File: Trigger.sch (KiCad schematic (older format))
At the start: 2 parts

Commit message: more
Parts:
- added C1, C2: C_Small, symbol Device:C_Small
- added J2: ARM_SWD, symbol MyComponents:ARM_SWD
- added U1: MCP6002, symbol MyComponents:MCP6002
- J1: renamed from J?; symbol dk_USB-DVI-HDMI-Connectors:UE27AC54100 -> Trigger-rescue:UE27AC54100-dk_USB-DVI-HDMI-Connectors
- U2: renamed from U?; symbol MyComponents:SAMD21E -> Trigger-rescue:SAMD21E-MyComponents
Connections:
- net labels added: 3V3, 5V, GND-power
- wire segments 2 -> 19
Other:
- note added: "Close to IC"
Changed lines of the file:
@@
 EESchema Schematic File Version 4
+LIBS:Trigger-cache
 EELAYER 26 0
 EELAYER END
@@
 $EndDescr
 $Comp
-L MyComponents:SAMD21E U?
+L Trigger-rescue:SAMD21E-MyComponents U2
 U 1 1 5C325D69
 P 4650 3400
-F 0 "U?" H 4650 2014 50  0000 C CNN
+F 0 "U2" H 4650 2014 50  0000 C CNN
 F 1 "SAMD21E" H 4650 1923 50  0000 C CNN
 F 2 "" H 4500 4400 50  0001 C CNN
@@
 $EndComp
 $Comp
-L dk_USB-DVI-HDMI-Connectors:UE27AC54100 J?
+L Trigger-rescue:UE27AC54100-dk_USB-DVI-HDMI-Connectors J1
 U 1 1 5C3264C2
 P 950 3600
-F 0 "J?" H 1069 4112 60  0000 C CNN
+F 0 "J1" H 1069 4112 60  0000 C CNN
 F 1 "UE27AC54100" H 1069 4006 60  0000 C CNN
 F 2 "digikey-footprints:USB_A_Female_UE27AC54100" H 1150 3800 60  0001 L CNN
@@
 DP
 $Comp
-L power:GND #PWR?
+L Trigger-rescue:GND-power #PWR01
 U 1 1 5C326690
 P 1250 4750
-F 0 "#PWR?" H 1250 4500 50  0001 C CNN
+F 0 "#PWR01" H 1250 4500 50  0001 C CNN
 F 1 "GND" H 1255 4577 50  0000 C CNN
 F 2 "" H 1250 4750 50  0001 C CNN
@@
 Text Label 1250 4750 0    50   ~ 0
 GND
-Wire Wire Line
-	4400 4700 4300 4700
-Wire Wire Line
-	4300 4700 4300 4950
-Connection ~ 4300 4700
-Text Label 4300 4950 0    50   ~ 0
-GND
 Text Label 4200 2350 0    50   ~ 0
 GND
+$Comp
+L MyComponents:MCP6002 U1
+U 1 1 5C37B7AA
+P 2500 6200
+F 0 "U1" H 3041 6253 60  0000 L CNN
+F 1 "MCP6002" H 3041 6147 60  0000 L CNN
+F 2 "" H 2500 6200 60  0000 C CNN
+F 3 "" H 2500 6200 60  0000 C CNN
+	1    2500 6200
+	1    0    0    -1
+$EndComp
+$Comp
+L MyComponents:MCP6002 U1
+U 2 1 5C37B8E3
+P 4400 6200
+F 0 "U1" H 4941 6253 60  0000 L CNN
+F 1 "MCP6002" H 4941 6147 60  0000 L CNN
+F 2 "" H 4400 6200 60  0000 C CNN
+F 3 "" H 4400 6200 60  0000 C CNN
+	2    4400 6200
+	1    0    0    -1
+$EndComp
+$Comp
+L Trigger-rescue:GND-power #PWR02
+U 1 1 5C37B973
+P 3500 6800
+F 0 "#PWR02" H 3500 6550 50  0001 C CNN
+F 1 "GND-power" H 3505 6627 50  0000 C CNN
+F 2 "" H 3500 6800 50  0001 C CNN
+F 3 "" H 3500 6800 50  0001 C CNN
+	1    3500 6800
+	1    0    0    -1
+$EndComp
+Wire Wire Line
+	2400 6600 3500 6600
+Wire Wire Line
+	3500 6600 3500 6800
+Wire Wire Line
+	3500 6600 4300 6600
+Connection ~ 3500 6600
+Text Label 4300 6600 0    50   ~ 0
+GND
+$Comp
+L MyComponents:ARM_SWD J2
+U 1 1 5C37BEB5
+P 1100 1750
+F 0 "J2" H 956 2358 60  0000 C CNN
+F 1 "ARM_SWD" H 956 2252 60  0000 C CNN
+F 2 "" H 1100 1750 60  0000 C CNN
+F 3 "" H 1100 1750 60  0000 C CNN
+	1    1100 1750
+	1    0    0    -1
+$EndComp
+Wire Wire Line
+	1300 1400 1400 1400
+Wire Wire Line
+	1500 1600 1500 1800
+Wire Wire Line
+	1300 1800 1500 1800
+Wire Wire Line
+	1300 1600 1500 1600
+Wire Wire Line
+	1500 1800 1500 2000
+Wire Wire Line
+	1300 2000 1500 2000
+Connection ~ 1500 1800
+Text Label 1500 1800 0    50   ~ 0
+GND
+Text Label 1400 1400 0    50   ~ 0
+3V3
+Wire Wire Line
+	4100 2350 4000 2350
+Wire Wire Line
+	4000 2200 4000 2350
+Connection ~ 4000 2350
+Text Label 4000 2200 0    50   ~ 0
+3V3
+Wire Wire Line
+	4400 4700 4400 4750
+Text Label 4400 4750 0    50   ~ 0
+GND
+Wire Wire Line
+	4300 4700 4300 4750
+Text Label 4300 4750 2    50   ~ 0
+3V3
+$Comp
+L Device:C_Small C1
+U 1 1 5C37CBD9
+P 1200 4500
+F 0 "C1" H 1292 4546 50  0000 L CNN
+F 1 "C_Small" H 1292 4455 50  0000 L CNN
+F 2 "" H 1200 4500 50  0001 C CNN
+F 3 "~" H 1200 4500 50  0001 C CNN
+	1    1200 4500
+	1    0    0    -1
+$EndComp
+$Comp
+L Device:C_Small C2
+U 1 1 5C37CC39
+P 1600 4500
+F 0 "C2" H 1692 4546 50  0000 L CNN
+F 1 "C_Small" H 1692 4455 50  0000 L CNN
+F 2 "" H 1600 4500 50  0001 C CNN
+F 3 "~" H 1600 4500 50  0001 C CNN
+	1    1600 4500
+	1    0    0    -1
+$EndComp
+Wire Wire Line
+	1250 4750 1250 4600
+Wire Wire Line
+	1250 4600 1200 4600
+Wire Wire Line
+	1250 4600 1600 4600
+Connection ~ 1250 4600
+Wire Wire Line
+	1200 4400 1200 4350
+Wire Wire Line
+	1200 4350 1600 4350
+Wire Wire Line
+	1600 4350 1600 4400
+Text Label 1200 4350 2    50   ~ 0
+3V3
+Text Notes 1800 4300 2    59   ~ 0
+Close to IC
+Text Label 4300 5800 0    59   ~ 0
+5V
+Text Label 2400 5800 0    59   ~ 0
+5V
 $EndSCHEMATC

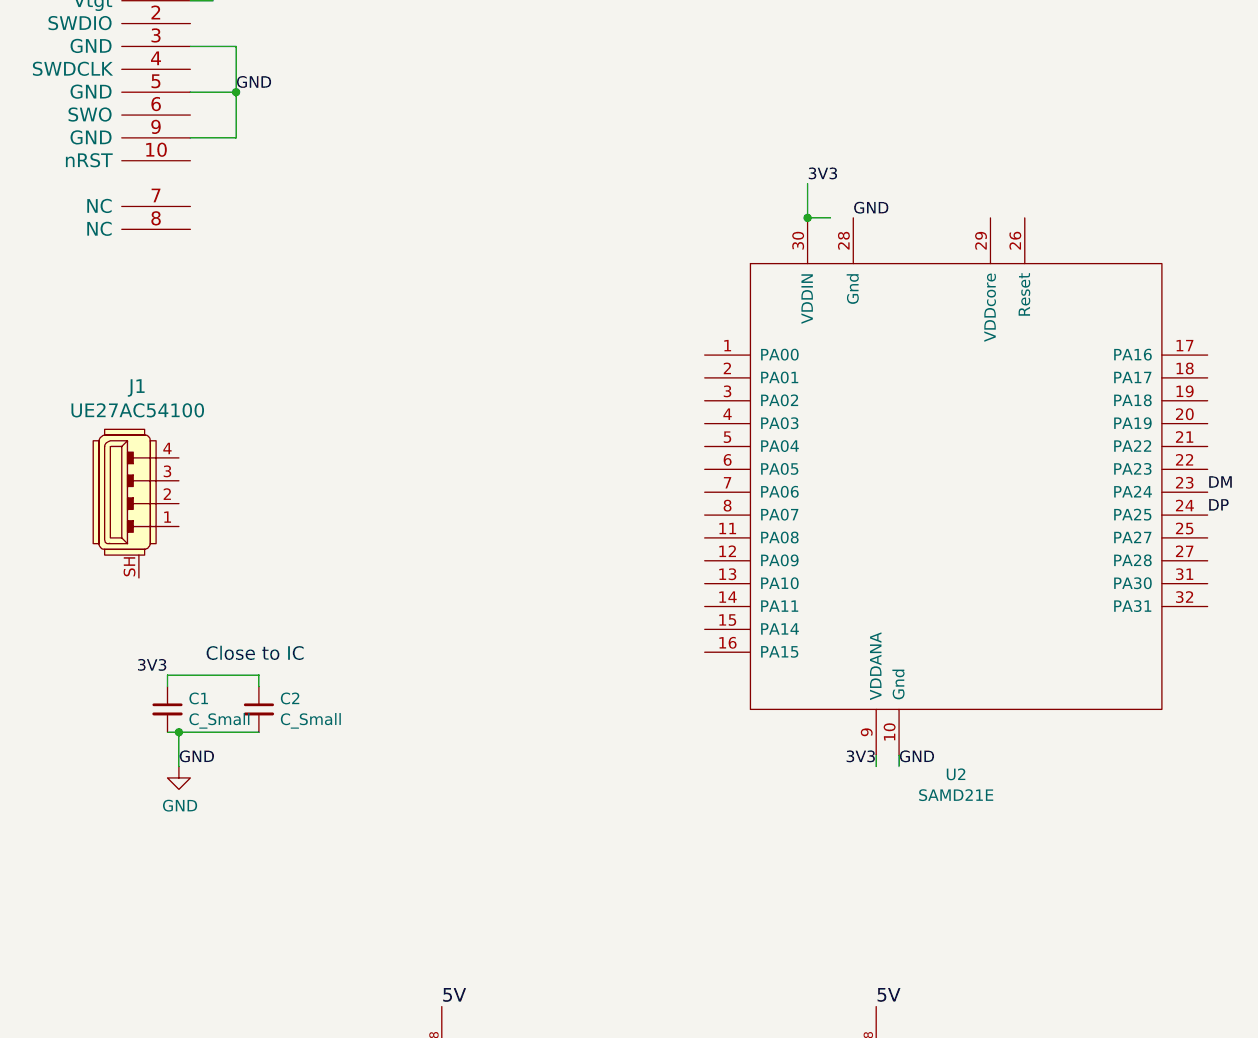
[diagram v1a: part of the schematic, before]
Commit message: corrected symbol samd and more connections
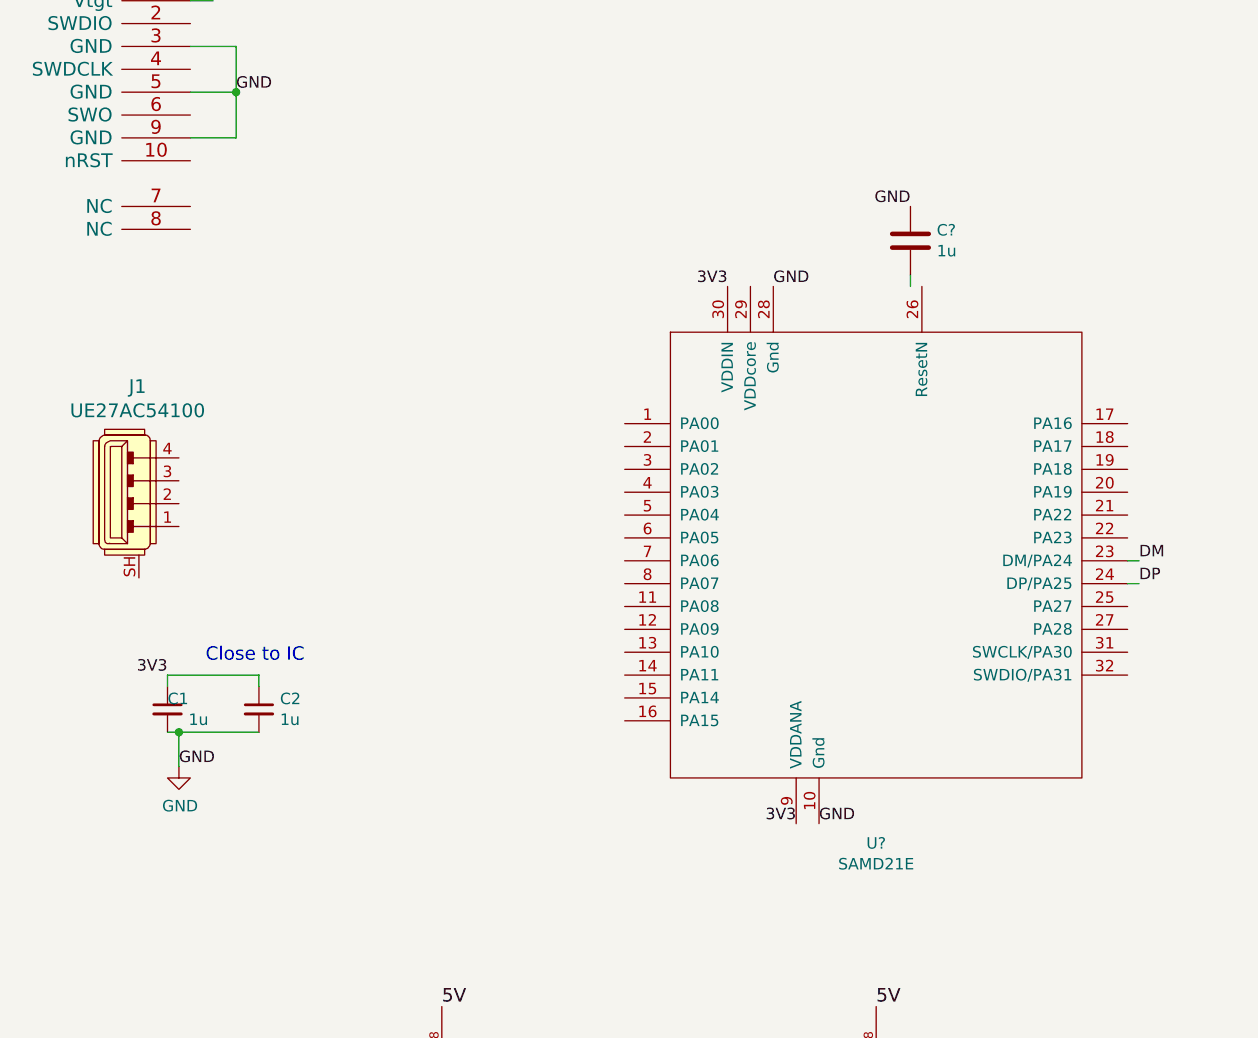
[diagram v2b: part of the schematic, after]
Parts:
- removed U2: SAMD21E, symbol Trigger-rescue:SAMD21E-MyComponents
- added C?: 1u, symbol Device:C
- added U?: SAMD21E, symbol MyComponents:SAMD21E
- C1, C2: value C_Small -> 1u
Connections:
- wire segments 19 -> 18
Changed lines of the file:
@@
 $EndDescr
-$Comp
-L Trigger-rescue:SAMD21E-MyComponents U2
-U 1 1 5C325D69
-P 4650 3400
-F 0 "U2" H 4650 2014 50  0000 C CNN
-F 1 "SAMD21E" H 4650 1923 50  0000 C CNN
-F 2 "" H 4500 4400 50  0001 C CNN
-F 3 "" H 4500 4400 50  0001 C CNN
-	1    4650 3400
-	1    0    0    -1
-$EndComp
 $Comp
 L Trigger-rescue:UE27AC54100-dk_USB-DVI-HDMI-Connectors J1
@@
 	1    0    0    -1
 $EndComp
-Text Label 5750 3550 0    50   ~ 0
+Text Label 5450 3850 0    50   ~ 0
 DM
-Text Label 5750 3650 0    50   ~ 0
+Text Label 5450 3950 0    50   ~ 0
 DP
 $Comp
@@
 $EndComp
 Text Label 1250 4750 0    50   ~ 0
-GND
-Text Label 4200 2350 0    50   ~ 0
 GND
 $Comp
@@
 Text Label 1400 1400 0    50   ~ 0
 3V3
-Wire Wire Line
-	4100 2350 4000 2350
-Wire Wire Line
-	4000 2200 4000 2350
-Connection ~ 4000 2350
-Text Label 4000 2200 0    50   ~ 0
-3V3
-Wire Wire Line
-	4400 4700 4400 4750
-Text Label 4400 4750 0    50   ~ 0
-GND
-Wire Wire Line
-	4300 4700 4300 4750
-Text Label 4300 4750 2    50   ~ 0
-3V3
 $Comp
 L Device:C_Small C1
 U 1 1 5C37CBD9
 P 1200 4500
-F 0 "C1" H 1292 4546 50  0000 L CNN
-F 1 "C_Small" H 1292 4455 50  0000 L CNN
+F 0 "C1" H 1292 4546 50  0000 R CNN
+F 1 "1u" H 1292 4455 50  0000 L CNN
 F 2 "" H 1200 4500 50  0001 C CNN
 F 3 "~" H 1200 4500 50  0001 C CNN
@@
 P 1600 4500
 F 0 "C2" H 1692 4546 50  0000 L CNN
-F 1 "C_Small" H 1692 4455 50  0000 L CNN
+F 1 "1u" H 1692 4455 50  0000 L CNN
 F 2 "" H 1600 4500 50  0001 C CNN
 F 3 "~" H 1600 4500 50  0001 C CNN
@@
 Text Label 2400 5800 0    59   ~ 0
 5V
+$Comp
+L MyComponents:SAMD21E U?
+U 1 1 5C3920CB
+P 4300 3700
+F 0 "U?" H 4300 2314 50  0000 C CNN
+F 1 "SAMD21E" H 4300 2223 50  0000 C CNN
+F 2 "" H 4150 4700 50  0001 C CNN
+F 3 "" H 4150 4700 50  0001 C CNN
+	1    4300 3700
+	1    0    0    -1
+$EndComp
+Text Label 4050 5000 0    50   ~ 0
+GND
+Text Label 3950 5000 2    50   ~ 0
+3V3
+Text Label 3850 2650 0    50   ~ 0
+GND
+Text Label 3650 2650 2    50   ~ 0
+3V3
+$Comp
+L Device:C C?
+U 1 1 5C3921F2
+P 4450 2450
+F 0 "C?" H 4565 2496 50  0000 L CNN
+F 1 "1u" H 4565 2405 50  0000 L CNN
+F 2 "" H 4488 2300 50  0001 C CNN
+F 3 "~" H 4450 2450 50  0001 C CNN
+	1    4450 2450
+	1    0    0    -1
+$EndComp
+Wire Wire Line
+	4450 2650 4450 2600
+Text Label 4450 2300 2    50   ~ 0
+GND
+Wire Wire Line
+	5400 3850 5450 3850
+Wire Wire Line
+	5400 3950 5450 3950
 $EndSCHEMATC

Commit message: progress
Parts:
- removed J1: UE27AC54100, digikey-footprints:USB_A_Female_UE27AC54100, symbol Trigger-rescue:UE27AC54100-dk_USB-DVI-HDMI-Connectors
- removed U?: SAMD21E, symbol MyComponents:SAMD21E
- added C4: 4u7, symbol Device:C_Small
- added C5: 1u, symbol Device:C_Small
- added C?: 1n, symbol Device:C_Small
- added D?: D_Photo, symbol Device:D_Photo
- added D? (x2): LED, symbol Device:LED
- added J?: USB_B_Micro, symbol Connector:USB_B_Micro
- added R? (x2): 100k, symbol Device:R
- added R? (x2): 10K, symbol Device:R
- added R?: 220R, symbol Device:R
- added RV?: 20k, symbol Device:R_POT
- added ResetN, SWCLK, SWDIO: TestPoint, symbol Connector:TestPoint
- added SW?: SW_SPST, symbol Switch:SW_SPST
- added U2: SAMD21E, symbol MyComponents:SAMD21E
- added U3: TPS769XX, symbol MyComponents:TPS769XX
- J2: symbol MyComponents:ARM_SWD -> Trigger-rescue:ARM_SWD-MyComponents
- U1: symbol MyComponents:MCP6002 -> Trigger-rescue:MCP6002-MyComponents
- gave numbers to parts that had none: 1
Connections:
- net labels added: RstN
- wire segments 18 -> 82
- no-connect marks 0 -> 2
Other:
- note added: "Position so can\nresolder"
- note added: "To Interupt"
- note added: "USB Connectors Farnell:\n2614950 = Molex 105017-10\nMaybe 2293836\nOther way up 2614947 = Molex 105164"
- moved on the sheet: C1, C2, C3

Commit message: progress
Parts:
- removed J2: ARM_SWD, symbol Trigger-rescue:ARM_SWD-MyComponents
- removed ResetN, SWCLK, SWDIO: TestPoint, symbol Connector:TestPoint
- added H? (x4): MountHole, symbol MyComponents:MountHole
- added J?: Screw_Terminal_01x06, symbol Connector:Screw_Terminal_01x06
- added J?: Conn_01x04_IO, symbol Connector:Conn_01x04_Female
- added U?: SWD_Pogo, symbol MyComponents:SWD_Pogo
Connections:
- net 3V3: now also RV?.1, U1.8 (V+), U1.8 (V+), J?.2 (Pin_2), U?.3 (Vtg)
- net 5V: now also J?.1 (Pin_1); no longer RV?.1, U1.8 (V+), U1.8 (V+)
- net GND: now also J?.1 (Pin_1), J?.6 (Pin_6), U?.1 (Gnd)
- net RstN: now also U?.5 (RstN)
- net SWCLK: now reaches U2.31 (SWCLK/PA30)
- net SWCLK: now also U?.4 (CLK)
- net SWDIO: now reaches U2.32 (SWDIO/PA31)
- net SWDIO: now also U?.2 (DIO)
- new net Flash: J?.4 (Pin_4)
- new net SW_FET: J?.5 (Pin_5)
- new net Trig: J?.3 (Pin_3)
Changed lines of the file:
@@
 GND
-$Comp
-L Trigger-rescue:ARM_SWD-MyComponents J2
-U 1 1 5C37BEB5
-P 1100 1750
-F 0 "J2" H 956 2358 60  0000 C CNN
-F 1 "ARM_SWD" H 956 2252 60  0000 C CNN
-F 2 "" H 1100 1750 60  0000 C CNN
-F 3 "" H 1100 1750 60  0000 C CNN
-	1    1100 1750
-	1    0    0    -1
-$EndComp
-Wire Wire Line
-	1300 1400 1400 1400
-Wire Wire Line
-	1500 1600 1500 1800
-Wire Wire Line
-	1300 1800 1500 1800
-Wire Wire Line
-	1300 1600 1500 1600
-Wire Wire Line
-	1500 1800 1500 2000
-Wire Wire Line
-	1300 2000 1500 2000
-Connection ~ 1500 1800
-Text Label 1500 1800 0    50   ~ 0
-GND
-Text Label 1400 1400 0    50   ~ 0
-3V3
 $Comp
 L Device:C_Small C1
@@
 Close to IC
 Text Label 4300 5800 0    59   ~ 0
-5V
+3V3
 Text Label 2400 5800 0    59   ~ 0
-5V
+3V3
 Text Label 4050 5000 0    50   ~ 0
 GND
@@
 	3900 5550 3900 6100
 Connection ~ 3900 6100
-$Comp
-L Connector:TestPoint SWDIO
-U 1 1 5C3CB332
-P 5700 4550
-F 0 "SWDIO" H 5642 4577 50  0000 R CNN
-F 1 "TestPoint" H 5642 4668 50  0000 R CNN
-F 2 "" H 5900 4550 50  0001 C CNN
-F 3 "~" H 5900 4550 50  0001 C CNN
-	1    5700 4550
-	-1   0    0    1
-$EndComp
-$Comp
-L Connector:TestPoint SWCLK
-U 1 1 5C3CB414
-P 6200 4550
-F 0 "SWCLK" H 6142 4577 50  0000 R CNN
-F 1 "TestPoint" H 6142 4668 50  0000 R CNN
-F 2 "" H 6400 4550 50  0001 C CNN
-F 3 "~" H 6400 4550 50  0001 C CNN
-	1    6200 4550
-	-1   0    0    1
-$EndComp
-$Comp
-L Connector:TestPoint ResetN
-U 1 1 5C3CB500
-P 6650 4550
-F 0 "ResetN" H 6592 4577 50  0000 R CNN
-F 1 "TestPoint" H 6592 4668 50  0000 R CNN
-F 2 "" H 6850 4550 50  0001 C CNN
-F 3 "~" H 6850 4550 50  0001 C CNN
-	1    6650 4550
-	-1   0    0    1
-$EndComp
-Wire Wire Line
-	5400 4350 5700 4350
-Wire Wire Line
-	5700 4350 5700 4550
-Wire Wire Line
-	5400 4250 6200 4250
-Wire Wire Line
-	6200 4250 6200 4550
 Text Label 5200 2650 0    50   ~ 0
 RstN
-Text Label 6650 4450 0    50   ~ 0
+$Comp
+L MyComponents:MountHole H?
+U 1 1 5C3B6A60
+P 650 7700
+F 0 "H?" H 790 7953 60  0000 L CNN
+F 1 "MountHole" H 790 7847 60  0000 L CNN
+F 2 "" H 650 7700 60  0001 C CNN
+F 3 "" H 650 7700 60  0001 C CNN
+	1    650  7700
+	1    0    0    -1
+$EndComp
+$Comp
+L MyComponents:MountHole H?
+U 1 1 5C3B6B94
+P 1000 7700
+F 0 "H?" H 1140 7953 60  0000 L CNN
+F 1 "MountHole" H 1140 7847 60  0000 L CNN
+F 2 "" H 1000 7700 60  0001 C CNN
+F 3 "" H 1000 7700 60  0001 C CNN
+	1    1000 7700
+	1    0    0    -1
+$EndComp
+$Comp
+L MyComponents:MountHole H?
+U 1 1 5C3B6C1C
+P 1350 7700
+F 0 "H?" H 1490 7953 60  0000 L CNN
+F 1 "MountHole" H 1490 7847 60  0000 L CNN
+F 2 "" H 1350 7700 60  0001 C CNN
+F 3 "" H 1350 7700 60  0001 C CNN
+	1    1350 7700
+	1    0    0    -1
+$EndComp
+$Comp
+L MyComponents:MountHole H?
+U 1 1 5C3B6C9A
+P 1700 7700
+F 0 "H?" H 1840 7953 60  0000 L CNN
+F 1 "MountHole" H 1840 7847 60  0000 L CNN
+F 2 "" H 1700 7700 60  0001 C CNN
+F 3 "" H 1700 7700 60  0001 C CNN
+	1    1700 7700
+	1    0    0    -1
+$EndComp
+$Comp
+L MyComponents:SWD_Pogo U?
+U 1 1 5C3BB35C
+P 2050 1750
+F 0 "U?" H 1896 2175 50  0000 C CNN
+F 1 "SWD_Pogo" H 1896 2084 50  0000 C CNN
+F 2 "" H 2300 1400 50  0001 C CNN
+F 3 "" H 2300 1400 50  0001 C CNN
+	1    2050 1750
+	1    0    0    -1
+$EndComp
+Wire Wire Line
+	2050 1550 2200 1550
+Text Label 2200 1550 0    50   ~ 0
+GND
+Wire Wire Line
+	2050 1750 2200 1750
+Wire Wire Line
+	2050 1650 2200 1650
+Wire Wire Line
+	2050 1850 2200 1850
+Wire Wire Line
+	2050 1950 2200 1950
+Text Label 2200 1950 0    50   ~ 0
 RstN
-Wire Wire Line
-	6650 4450 6650 4550
+Text Label 2200 1850 0    50   ~ 0
+SWCLK
+Text Label 2200 1750 0    50   ~ 0
+3V3
+Text Label 2200 1650 0    50   ~ 0
+SWDIO
+Text Label 5400 4350 0    50   ~ 0
+SWDIO
+Text Label 5400 4250 0    50   ~ 0
+SWCLK
+Text Label 7800 3650 0    50   ~ 0
+GND
+Text Label 7800 4150 0    50   ~ 0
+5V
+Text Label 7800 4050 0    50   ~ 0
+3V3
+Text Label 7800 3750 0    50   ~ 0
+SW_FET
+Text Label 7800 3850 0    50   ~ 0
+Flash
+Text Label 7800 3950 0    50   ~ 0
+Trig
+$Comp
+L Connector:Screw_Terminal_01x06 J?
+U 1 1 5C3CC01B
+P 7600 3950
+F 0 "J?" H 7520 3425 50  0000 C CNN
+F 1 "Screw_Terminal_01x06" H 7520 3516 50  0000 C CNN
+F 2 "" H 7600 3950 50  0001 C CNN
+F 3 "~" H 7600 3950 50  0001 C CNN
+	1    7600 3950
+	-1   0    0    1
+$EndComp
+$Comp
+L Connector:Conn_01x04_Female J?
+U 1 1 5C3D094F
+P 7600 4550
+F 0 "J?" H 7628 4526 50  0000 L CNN
+F 1 "Conn_01x04_IO" H 7628 4435 50  0000 L CNN
+F 2 "" H 7600 4550 50  0001 C CNN
+F 3 "~" H 7600 4550 50  0001 C CNN
+	1    7600 4550
+	1    0    0    -1
+$EndComp
+Text Label 7400 4450 2    50   ~ 0
+GND
 $EndSCHEMATC
